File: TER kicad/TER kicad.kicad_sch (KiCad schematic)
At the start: 6 parts, among them U1 74AHC1G14, U2 CH340C

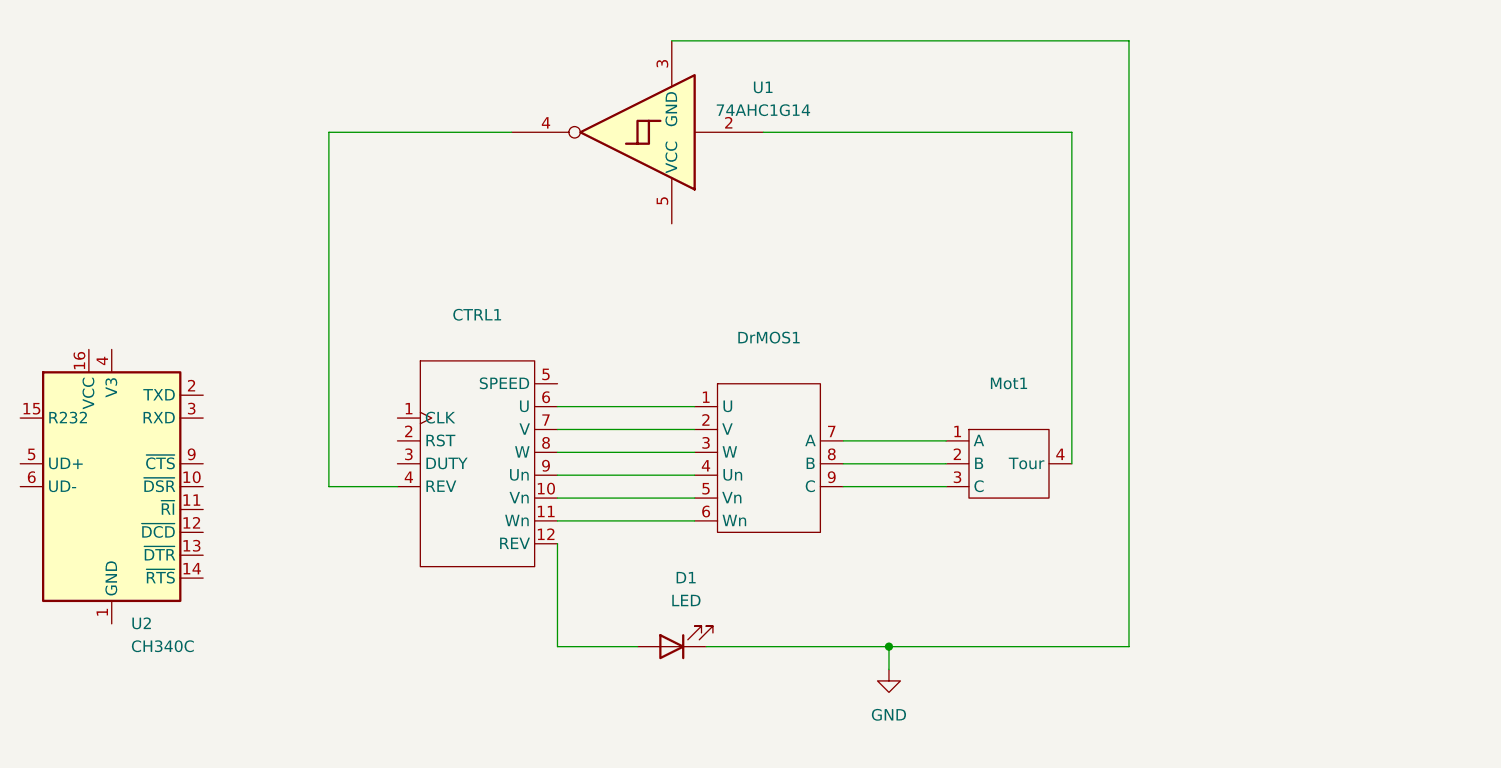
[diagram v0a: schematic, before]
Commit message: Rework : changement du pont en H sur Kicad
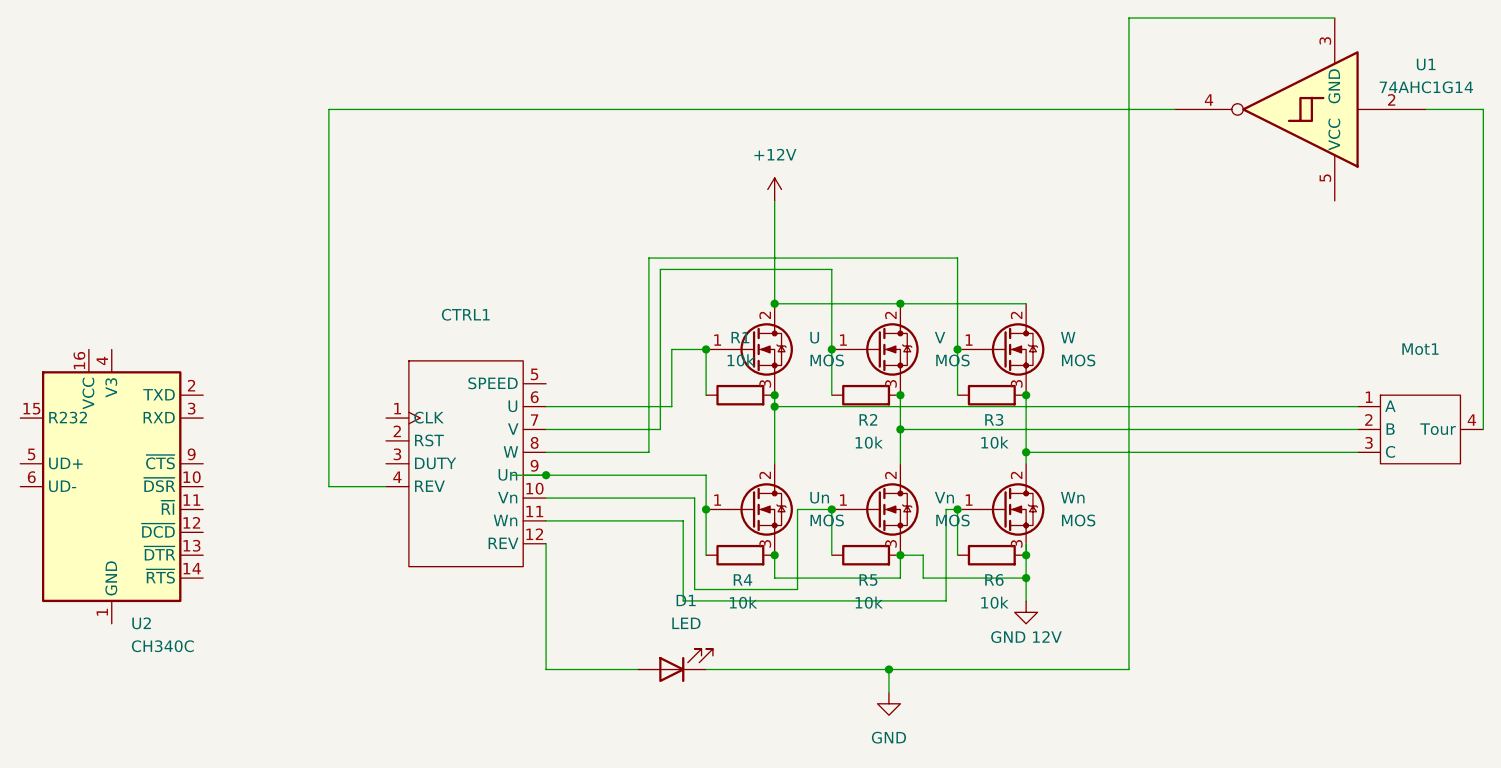
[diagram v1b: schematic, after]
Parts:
- removed DrMOS1: ~, symbol custom:Driver_Mosfet
- added R1, R2, R3, R4, R5, R6: 10k, symbol Device:R
- added U, Un, V, Vn, W, Wn: MOS, Package_TO_SOT_THT:TO-220-3_Vertical, symbol Transistor_FET:IRLB8721PBF
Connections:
- net at CTRL1.10 (Vn): now also R5.1, Vn.1 (G)
- net at CTRL1.11 (Wn): now also R6.1, Wn.1 (G)
- net at CTRL1.6 (U): now also R1.1, U.1 (G)
- net at CTRL1.7 (V): now also R2.1, V.1 (G)
- net at CTRL1.8 (W): now also R3.1, W.1 (G)
- net at CTRL1.9 (Un): now also R4.1, Un.1 (G)
- net at Mot1.1 (A): now also R1.2, U.3 (S), Un.2 (D)
- net at Mot1.2 (B): now also R2.2, V.3 (S), Vn.2 (D)
- net at Mot1.3 (C): now also R3.2, W.3 (S), Wn.2 (D)
- new net +12V: U.2 (D), V.2 (D), W.2 (D)
- new net GND 12V: R4.2, R5.2, R6.2, Un.3 (S), Vn.3 (S), Wn.3 (S)
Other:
- moved on the sheet: CTRL1, D1, Mot1, U1

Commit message: Feat: V0 du PCB
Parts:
- removed U2: CH340C, Package_SO:SOIC-16_3.9x9.9mm_P1.27mm, symbol Interface_USB:CH340C
- added J1: Conn_01x06_Pin, Connector_PinSocket_2.54mm:PinSocket_1x06_P2.54mm_Vertical, symbol Connector:Conn_01x06_Pin
- added J2: Conn_01x02_Pin, Connector_PinSocket_2.00mm:PinSocket_1x02_P2.00mm_Vertical, symbol Connector:Conn_01x02_Pin
- Mot1: footprint (none) -> Connector_PinSocket_2.00mm:PinSocket_1x03_P2.00mm_Vertical
- R1, R2, R3, R4, R5, R6: footprint (none) -> Resistor_THT:R_Axial_DIN0204_L3.6mm_D1.6mm_P5.08mm_Horizontal
- renumbered U to U3, Un to Un1, V to V1, Vn to Vn1, W to W1, Wn to Wn1
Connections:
- net +12V: now also J2.2 (Pin_2)
- net GND 12V: now also J2.1 (Pin_1)
- net at CTRL1.10 (Vn), R5.1, Vn1.1 (G): now also J1.5 (Pin_5)
- net at CTRL1.11 (Wn), R6.1, Wn1.1 (G): now also J1.6 (Pin_6)
- net at CTRL1.6 (U), R1.1, U3.1 (G): now also J1.1 (Pin_1)
- net at CTRL1.7 (V), R2.1, V1.1 (G): now also J1.2 (Pin_2)
- net at CTRL1.8 (W), R3.1, W1.1 (G): now also J1.3 (Pin_3)
- net at CTRL1.9 (Un), R4.1, Un1.1 (G): now also J1.4 (Pin_4)
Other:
- moved on the sheet: CTRL1
